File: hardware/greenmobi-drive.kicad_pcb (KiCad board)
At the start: 2 copper layers, 100 x 100 mm, 149 parts, among them J1 GND, J10 Motor NTC, J2 Encoder/Hall, J3 UBAT, J4 USB_C_Receptacle_USB2.0_14P, J5 CAN, J6 Debug, J7 Phase_OUT, J8 Phase_OUT, J9 Phase_OUT, Q3 IPT015N10N5, Q4 IPT015N10N5, Q5 IPT015N10N5, Q6 IPT015N10N5, Q7 IPT015N10N5, Q8 IPT015N10N5, SW1 BOOT, SW2 RESET, U1 BMI323, U10 TPS54202DDC, U11 LM5163DDA, U12 AMS1117-3.3, U2 TJA1051T-3, U3 STM32F405RGTx, U4 IRS21867S, U5 INA240A2D, U6 IRS21867S, U7 INA240A2D, U8 IRS21867S, U9 INA240A2D, Y1 8MHz

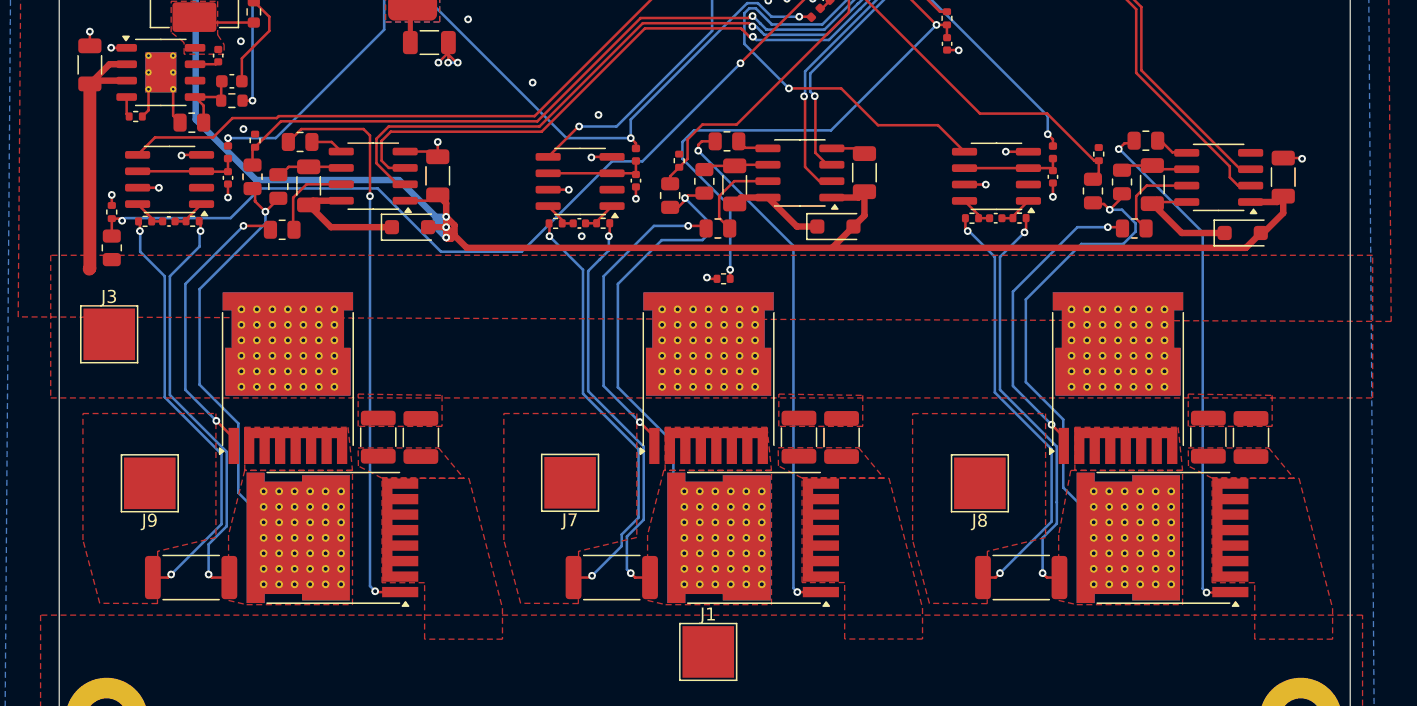
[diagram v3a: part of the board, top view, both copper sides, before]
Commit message: TVS and eletrolythic cap
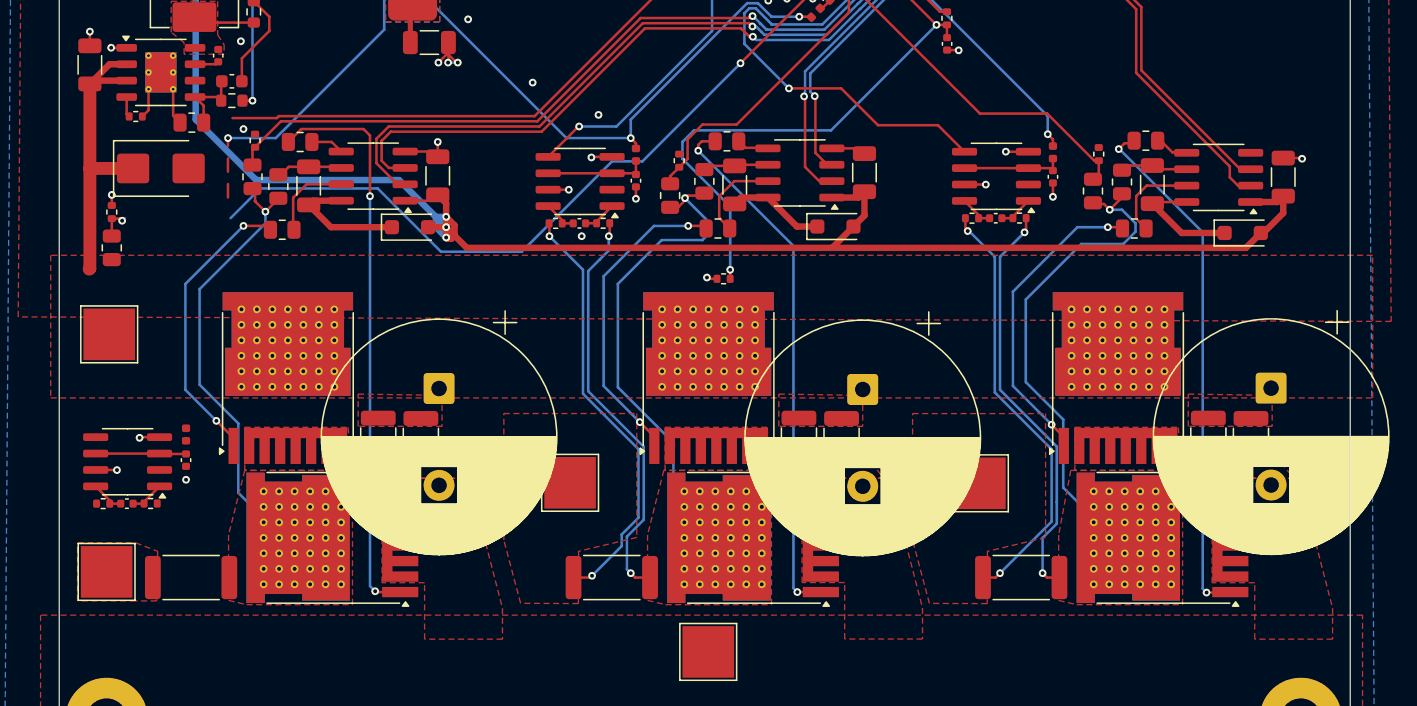
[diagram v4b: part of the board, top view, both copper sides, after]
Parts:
- added C308: 820uF, Capacitor_THT:CP_Radial_D18.0mm_P7.50mm, F.Cu at (156.2, 116.7)
- added C408: 820uF, Capacitor_THT:CP_Radial_D18.0mm_P7.50mm, F.Cu at (187.8, 116.6)
- added C508: 820uF, Capacitor_THT:CP_Radial_D18.0mm_P7.50mm, F.Cu at (123.3, 116.6)
- added D101: SM6T56A, Diode_SMD:D_SMB, F.Cu at (101.8, 99.5)
- L602: renamed from L6; value 6.8u -> 68u
- R301: renamed from R18; value 1 -> 4.7
- R308: renamed from R24; value 1 -> 10
- R309: renamed from R25; value 1 -> 10
- R401: renamed from R26; value 1 -> 4.7
- R408: renamed from R32; value 1 -> 10
- R409: renamed from R33; value 1 -> 10
- R501: renamed from R34; value 1 -> 4.7
- R508: renamed from R40; value 1 -> 10
- R509: renamed from R41; value 1 -> 10
- moved C504 22.1 mm to (103.8, 122.1)
- moved C505 22.1 mm to (99.2, 125.5)
- moved L501 22.1 mm to (103.8, 120.2)
- moved R505 22.1 mm to (97.3, 125.5)
- moved R507 22.1 mm to (101.0, 125.5)
- moved U502 22.1 mm to (99.2, 122.3)
- moved J501 7.63 mm to (97.6, 130.8)
- renumbered C1 to C101, C2 to C102, C4 to C103, C3 to C104, C5 to C105, C6 to C106, C7 to C201, C8 to C202, C9 to C203, C10 to C204, C11 to C205, C12 to C206, C13 to C207, C14 to C208, C15 to C209, C16 to C210, C17 to C211, C18 to C212, C19 to C213, C20 to C301, C21 to C302, C22 to C304, C23 to C305, C24 to C306, C25 to C307, C26 to C401, C27 to C402, C28 to C404, C29 to C405, C30 to C406, C31 to C407, C32 to C501, C33 to C502, C34 to C504, C35 to C505, C36 to C506, C37 to C507, C38 to C601, C39 to C602, C40 to C603, C41 to C604, C42 to C605, C43 to C606, C44 to C607, C45 to C608, C46 to C609, C47 to C610, C48 to C611, C49 to C612, C50 to C613, C51 to C614, D1 to D102, D7 to D103, D3 to D104, D4 to D301, D5 to D401, D6 to D501, H1 to H201, H2 to H202, H3 to H203, H4 to H204, J3 to J101, J1 to J102, J2 to J103, J10 to J104, J4 to J105, J5 to J106, J6 to J201, J7 to J301, J8 to J401, J9 to J501, L1 to L201, L2 to L301, L3 to L401, L4 to L501, L5 to L601, Q3 to Q301, Q4 to Q302, Q5 to Q401, Q6 to Q402, Q7 to Q501, Q8 to Q502, R2 to R101, R3 to R102, R4 to R103, R5 to R104, R6 to R105, R7 to R106, R8 to R107, R9 to R108, R42 to R109, R12 to R110, R10 to R111, R1 to R112, R11 to R113, R13 to R114, R14 to R115, R16 to R201, R17 to R202, R15 to R203, R49 to R204, R19 to R302, R20 to R303, R21 to R305, R22 to R306, R23 to R307, R27 to R402, R28 to R403, R29 to R405, R30 to R406, R31 to R407, R35 to R502, R36 to R503, R37 to R505, R38 to R506, R39 to R507, R43 to R601, R44 to R602, R45 to R603, R46 to R604, R47 to R605, R48 to R606, SW1 to SW201, SW2 to SW202, TH1 to TH101, U1 to U101, U2 to U102, U3 to U201, U4 to U301, U5 to U302, U6 to U401, U7 to U402, U8 to U501, U9 to U502, U10 to U601, U11 to U602, U12 to U603, Y1 to Y201
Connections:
- C302 pad 1: Net-(D4-K) -> /half-bridge/HS
- C402 pad 1: Net-(D5-K) -> /half-bridge1/HS
- C502 pad 1: Net-(D6-K) -> /half-bridge2/HS
- D301 pad 1: Net-(D4-K) -> /half-bridge/HS
- D401 pad 1: Net-(D5-K) -> /half-bridge1/HS
- D501 pad 1: Net-(D6-K) -> /half-bridge2/HS
- J201 pad 8: /mcu/TDI -> unconnected-(J201-NC/TDI-Pad8)
- J301 pad 1: Net-(J7-Pin_1) -> Net-(J301-Pin_1)
- J401 pad 1: Net-(J8-Pin_1) -> Net-(J401-Pin_1)
- J501 pad 1: Net-(J9-Pin_1) -> Net-(J501-Pin_1)
- Q301 pad 2: /half-bridge/Center -> Net-(Q301-S)
- Q302 pad 3: /half-bridge/Center -> Net-(Q301-S)
- Q401 pad 2: /half-bridge1/Center -> Net-(Q401-S)
- Q402 pad 3: /half-bridge1/Center -> Net-(Q401-S)
- Q501 pad 2: /half-bridge2/Center -> Net-(Q501-S)
- Q502 pad 3: /half-bridge2/Center -> Net-(Q501-S)
- R301 pad 2: /half-bridge/Center -> Net-(Q301-S)
- R302 pad 2: /half-bridge/Center -> Net-(J301-Pin_1)
- R305 pad 2: Net-(J7-Pin_1) -> Net-(Q301-S)
- R306 pad 1: /half-bridge/Center -> Net-(Q301-S)
- R306 pad 2: Net-(J7-Pin_1) -> Net-(J301-Pin_1)
- R307 pad 2: /half-bridge/Center -> Net-(J301-Pin_1)
- R401 pad 2: /half-bridge1/Center -> Net-(Q401-S)
- R402 pad 2: /half-bridge1/Center -> Net-(J401-Pin_1)
- R405 pad 2: Net-(J8-Pin_1) -> Net-(Q401-S)
- R406 pad 1: /half-bridge1/Center -> Net-(Q401-S)
- R406 pad 2: Net-(J8-Pin_1) -> Net-(J401-Pin_1)
- R407 pad 2: /half-bridge1/Center -> Net-(J401-Pin_1)
- R501 pad 2: /half-bridge2/Center -> Net-(Q501-S)
- R502 pad 2: /half-bridge2/Center -> Net-(J501-Pin_1)
- R505 pad 2: Net-(J9-Pin_1) -> Net-(Q501-S)
- R506 pad 1: /half-bridge2/Center -> Net-(Q501-S)
- R506 pad 2: Net-(J9-Pin_1) -> Net-(J501-Pin_1)
- R507 pad 2: /half-bridge2/Center -> Net-(J501-Pin_1)
- U301 pad 8: Net-(D4-K) -> /half-bridge/HS
- U302 pad 5: /half-bridge/Current_sense -> Net-(R304-Pad2)
- U401 pad 8: Net-(D5-K) -> /half-bridge1/HS
- U402 pad 5: /half-bridge1/Current_sense -> Net-(R404-Pad2)
- U501 pad 8: Net-(D6-K) -> /half-bridge2/HS
- U502 pad 5: /half-bridge2/Current_sense -> Net-(R504-Pad2)
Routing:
- net (no net): track 0.00 -> 240.3 mm, vias 0 -> 11
- net /half-bridge1/Center: track 70.3 -> 0.00 mm, vias 3 -> 0
- net /half-bridge/Center: track 69.7 -> 0.00 mm, vias 3 -> 0
- net /half-bridge2/Center: track 66.3 -> 0.00 mm, vias 3 -> 0
- net Net-(J8-Pin_1): track 33.4 -> 0.00 mm, vias 2 -> 0
- net Net-(J7-Pin_1): track 33.1 -> 0.00 mm, vias 2 -> 0
- net Net-(J9-Pin_1): track 33.1 -> 0.00 mm, vias 2 -> 0
- net Net-(D6-K): track 9.82 -> 0.00 mm
- net /half-bridge2/HS: track 6.66 -> 16.5 mm
- net /half-bridge1/HS: track 7.07 -> 16.1 mm
- net Net-(D5-K): track 9.00 -> 0.00 mm
- net /half-bridge2/Current_sense: track 65.7 -> 57.1 mm
- net /mcu/Vin: track 70.9 -> 62.7 mm
- net Net-(D4-K): track 7.53 -> 0.00 mm
- net /half-bridge/HS: track 7.09 -> 14.6 mm
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- added copper zone on F.Cu, net Net-(J301-Pin_1)
- added copper zone on F.Cu, net Net-(J401-Pin_1)
- added copper zone on F.Cu, net Net-(J501-Pin_1)
- added copper zone on F.Cu, net Net-(Q301-S)
- added copper zone on F.Cu, net Net-(Q401-S)
- added copper zone on F.Cu, net Net-(Q501-S)
- removed copper zone on F.Cu, net /half-bridge/Center
- removed copper zone on F.Cu, net /half-bridge1/Center
- removed copper zone on F.Cu, net /half-bridge2/Center
- removed copper zone on F.Cu, net Net-(J7-Pin_1)
- removed copper zone on F.Cu, net Net-(J8-Pin_1)
- removed copper zone on F.Cu, net Net-(J9-Pin_1)

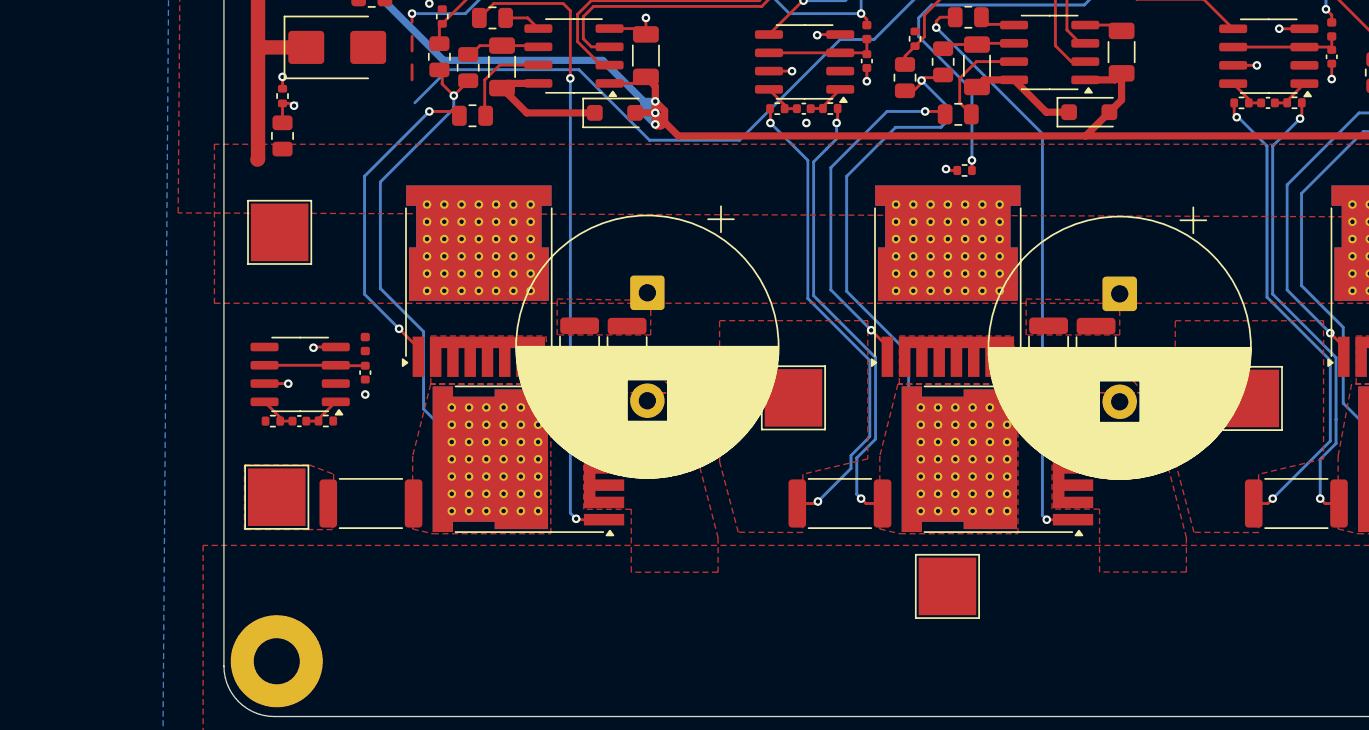
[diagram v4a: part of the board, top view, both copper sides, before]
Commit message: Change solder wire pads
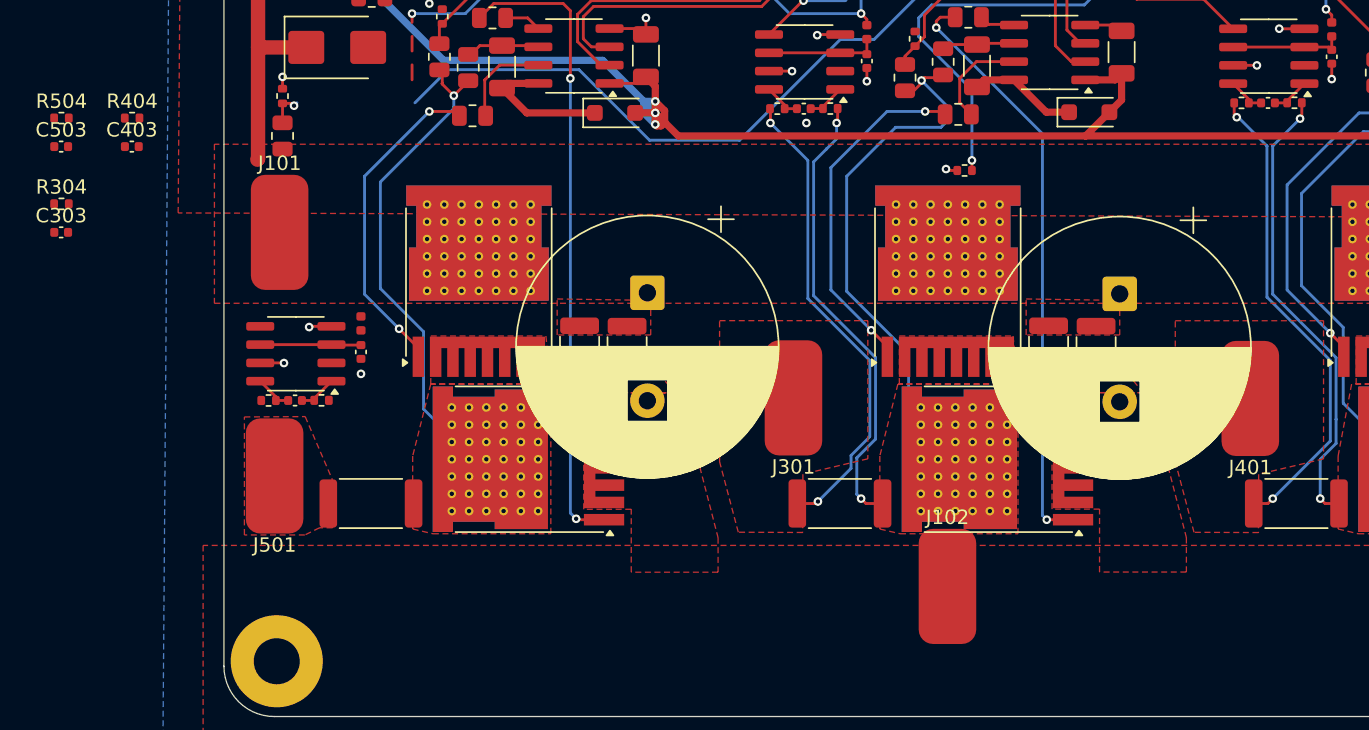
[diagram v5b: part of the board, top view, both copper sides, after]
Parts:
- added C303: 1n, Capacitor_SMD:C_0402_1005Metric, F.Cu at (82.6, 112.4)
- added C403: 1n, Capacitor_SMD:C_0402_1005Metric, F.Cu at (87.5, 106.4)
- added C503: 1n, Capacitor_SMD:C_0402_1005Metric, F.Cu at (82.6, 106.4)
- added R304: 1k, Resistor_SMD:R_0402_1005Metric, F.Cu at (82.6, 110.4)
- added R404: 1k, Resistor_SMD:R_0402_1005Metric, F.Cu at (87.5, 104.5)
- added R504: 1k, Resistor_SMD:R_0402_1005Metric, F.Cu at (82.6, 104.5)
- J101, J102, J301, J401, J501: footprint TestPoint:TestPoint_Pad_4.0x4.0mm -> Connector_Wire:SolderWirePad_1x01_SMD_4x8mm
- moved J501 1.48 mm to (97.5, 129.3)
- moved R507 1.47 mm to (100.7, 124.1)
- moved C504 1.47 mm to (103.5, 120.7)
- moved C505 1.47 mm to (98.9, 124.1)
- moved L501 1.47 mm to (103.5, 118.7)
- moved R505 1.47 mm to (97.0, 124.1)
- moved U502 1.47 mm to (98.9, 120.8)

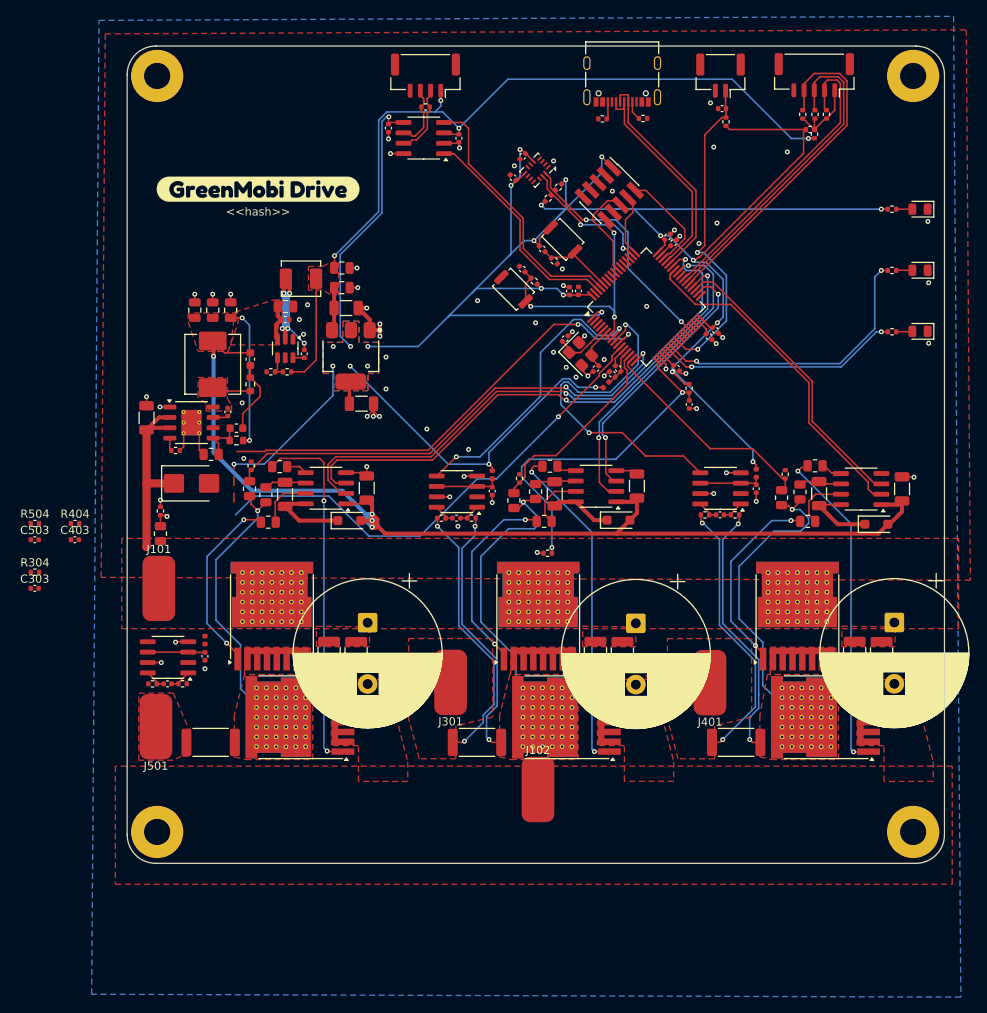
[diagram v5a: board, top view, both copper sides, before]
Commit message: Added external analog inputs
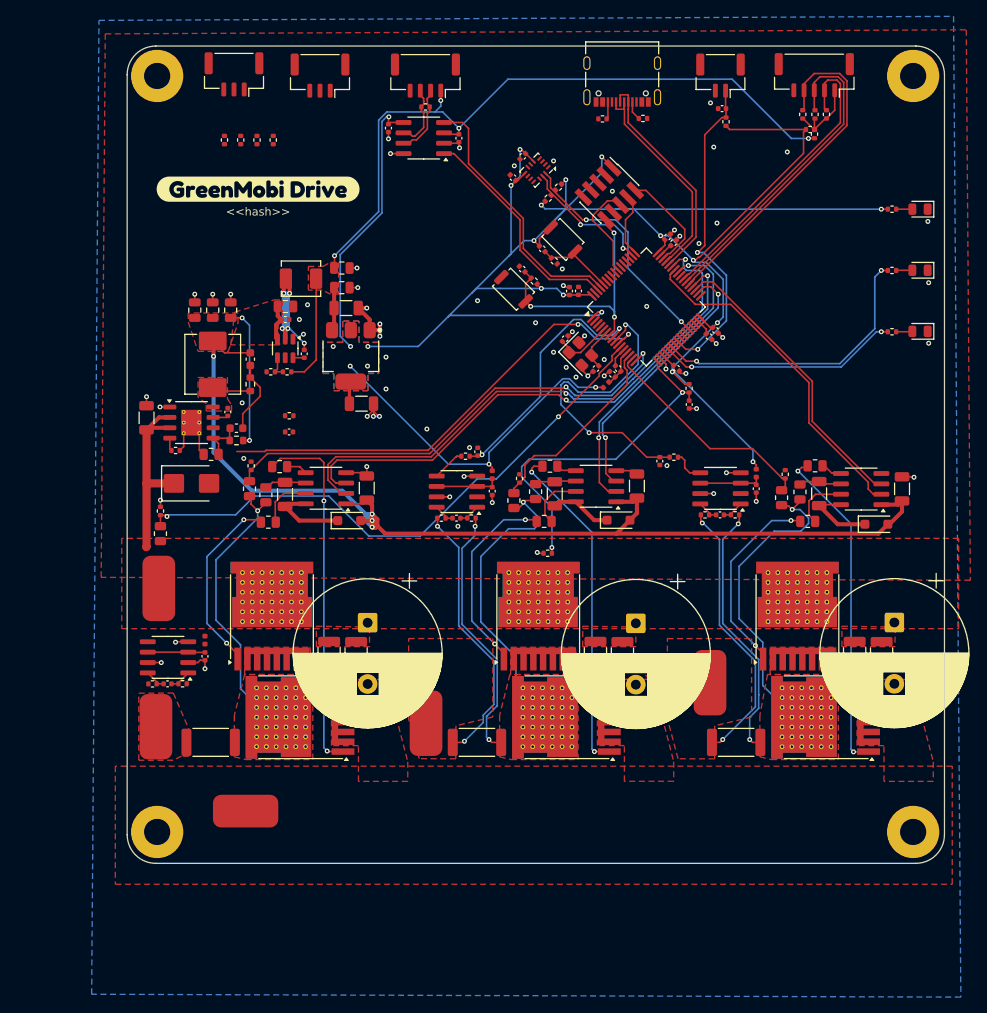
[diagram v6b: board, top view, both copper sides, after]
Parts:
- added J107: ADC, Connector_JST:JST_GH_SM03B-GHS-TB_1x03-1MP_P1.25mm_Horizontal, F.Cu at (107.0, 49.5)
- added J108: ADC, Connector_JST:JST_GH_SM03B-GHS-TB_1x03-1MP_P1.25mm_Horizontal, F.Cu at (117.5, 49.6)
- added R116: 0, Resistor_SMD:R_0402_1005Metric, F.Cu at (105.8, 57.5)
- added R117: 0, Resistor_SMD:R_0402_1005Metric, F.Cu at (107.8, 57.5)
- added R118: 0, Resistor_SMD:R_0402_1005Metric, F.Cu at (109.8, 57.5)
- added R119: 0, Resistor_SMD:R_0402_1005Metric, F.Cu at (111.8, 57.5)
- moved R404 73.7 mm to (160.8, 96.3)
- moved C403 72.2 mm to (159.1, 96.8), turned to -90 degrees
- moved C303 56.7 mm to (136.8, 95.7), turned to 90 degrees
- moved R304 54.6 mm to (135.3, 96.2), turned to 180 degrees
- moved J102 35.9 mm to (108.4, 139.7), turned to -90 degrees
- moved R504 33.8 mm to (113.8, 91.3)
- moved C503 33.8 mm to (113.7, 93.3)
- moved J301 5.83 mm to (130.5, 128.9)
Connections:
- net /CAN_N renamed /Interfaces/CAN_N
- net /CAN_P renamed /Interfaces/CAN_P
- net /USB_DN renamed /Interfaces/USB_DN
- net /USB_DP renamed /Interfaces/USB_DP
- net /mcu/CAN_RX renamed /Interfaces/CAN_RX
- net /mcu/CAN_TX renamed /Interfaces/CAN_TX
- C302 pad 1: /half-bridge/HS -> Net-(D301-K)
- C402 pad 1: /half-bridge1/HS -> Net-(D401-K)
- C502 pad 1: /half-bridge2/HS -> Net-(D501-K)
- D301 pad 1: /half-bridge/HS -> Net-(D301-K)
- D401 pad 1: /half-bridge1/HS -> Net-(D401-K)
- D501 pad 1: /half-bridge2/HS -> Net-(D501-K)
- U201 pad 20: unconnected-(U201-PA4-Pad20) -> /mcu/EXT_ANALOG_1
- U201 pad 23: unconnected-(U201-PA7-Pad23) -> /mcu/EXT_ANALOG_2
- U301 pad 8: /half-bridge/HS -> Net-(D301-K)
- U401 pad 8: /half-bridge1/HS -> Net-(D401-K)
- U501 pad 8: /half-bridge2/HS -> Net-(D501-K)
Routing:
- net +3.3V: track 338.7 -> 318.9 mm, vias 25 -> 23
- net Net-(D501-K): track 0.00 -> 9.82 mm
- net /half-bridge2/HS: track 16.5 -> 6.66 mm
- net /half-bridge1/HS: track 16.1 -> 7.07 mm
- net Net-(D401-K): track 0.00 -> 9.00 mm
- net /mcu/Vin: track 62.7 -> 70.9 mm
- net Net-(D301-K): track 0.00 -> 7.53 mm
- net /half-bridge/HS: track 14.6 -> 7.09 mm
- net /half-bridge/Current_sense: track 36.1 -> 31.1 mm
- net /half-bridge1/Current_sense: track 42.6 -> 38.1 mm
- net Net-(R404-Pad2): track 0.00 -> 4.05 mm
- net Net-(R304-Pad2): track 0.00 -> 4.02 mm
- net GND: track 67.9 -> 70.1 mm, vias 71 -> 72
- net Net-(U502-REF2): track 8.03 -> 7.01 mm
